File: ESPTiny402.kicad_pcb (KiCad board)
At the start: 2 copper layers, 26.4 x 23.9 mm, 20 parts, among them J1 Conn_01x10_Male, J2 Conn_01x10_Male, J3 Conn_01x04_Male, U1 ESP-01v090, U2 ATtiny402-SS, U3 MCP1700

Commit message: Minor layout changes
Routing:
- net GND: track 125.0 -> 119.9 mm

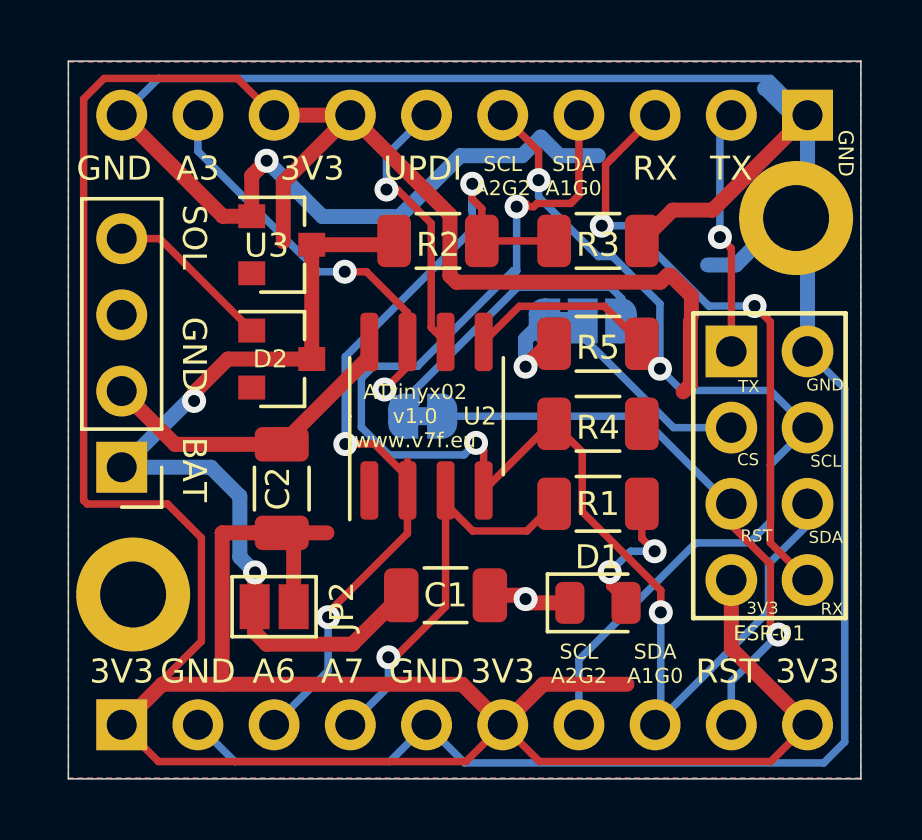
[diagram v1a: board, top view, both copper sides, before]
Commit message: Led to 1206 size
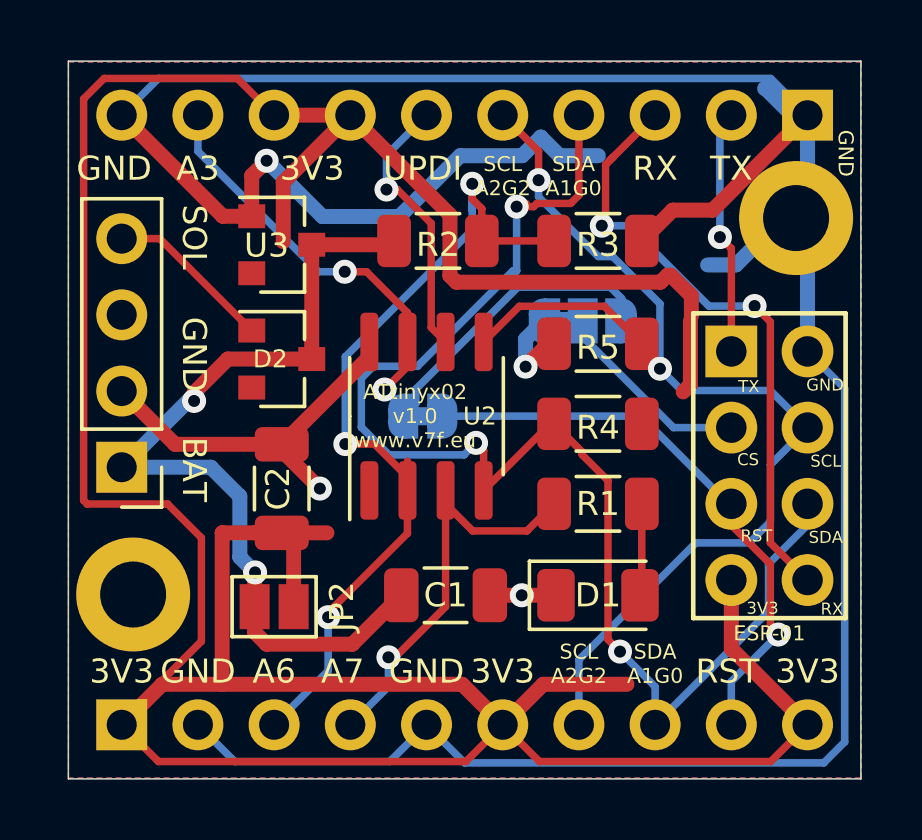
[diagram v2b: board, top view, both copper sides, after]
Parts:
- D1: footprint LED_SMD:LED_0805_2012Metric -> LED_SMD:LED_1206_3216Metric
- moved D1 0.25 mm to (63.4, 58.2)
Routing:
- net Net-(D1-Pad2): track 4.79 -> 3.07 mm, vias 2 -> 0
- net GND: track 119.9 -> 121.3 mm, vias 2 -> 3

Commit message: Minor routing updates
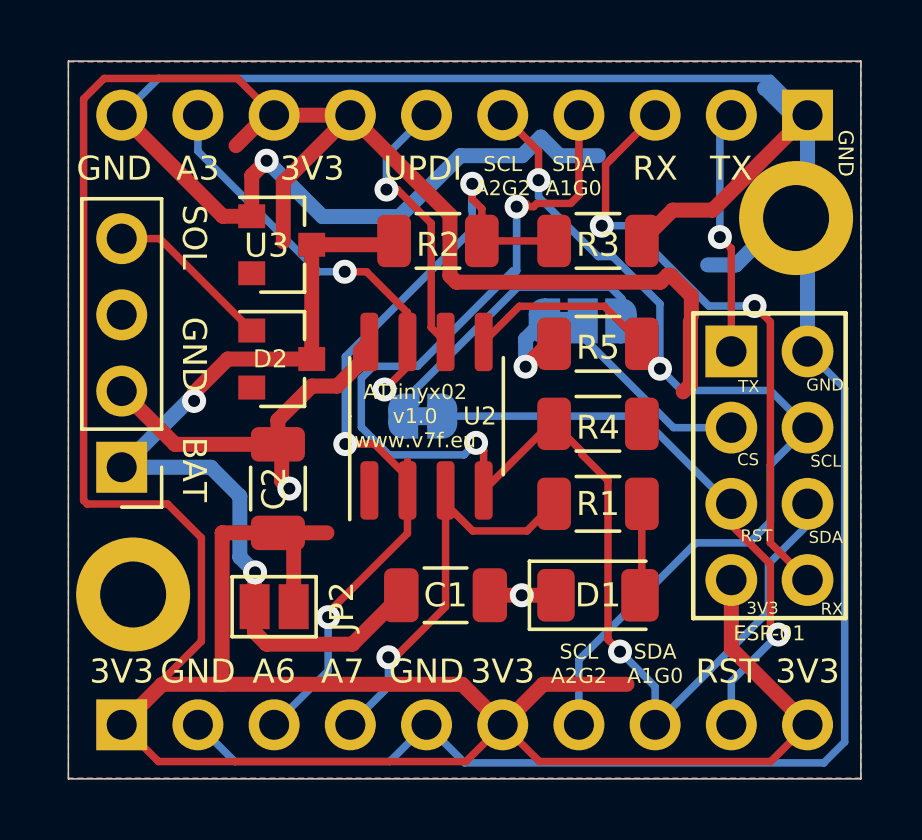
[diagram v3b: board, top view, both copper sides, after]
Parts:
- moved C2 0.13 mm to (52.7, 54.6)
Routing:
- net +3V3: track 123.0 -> 124.7 mm
- net GND: track 121.3 -> 122.1 mm
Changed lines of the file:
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@@
     (thickness 1.6)
     (drawings 55)
-    (tracks 271)
+    (tracks 279)
     (zones 0)
     (modules 20)
@@
   )
   (module Capacitor_SMD:C_1206_3216Metric (layer F.Cu)
-    (at 52.832 54.61 90)
+    (at 52.705 54.61 90)
     (descr "Capacitor SMD 1206 (3216 Metric), square (rectangular) end terminal, IPC_7351 nominal, (Body size source: IPC-SM-782 page 76, https://www.pcb-3d.com/wordpress/wp-content/uploads/ipc-sm-782a_amendment_1_and_2.pdf), generated with kicad-footprint-generator")
     (tags capacitor)
@@
   (segment (start 47.498 51.3588) (end 49.2742 53.135) (width 0.5) (layer F.Cu) (net 1) (status 10))
   (segment (start 55.753 50.214) (end 55.753 49.722) (width 0.5) (layer F.Cu) (net 1) (status 30))
-  (segment (start 52.832 53.135) (end 55.753 50.214) (width 0.5) (layer F.Cu) (net 1) (status 30))
   (segment (start 50.866 45.532) (end 51.832 45.532) (width 0.5) (layer F.Cu) (net 1) (status 20))
   (segment (start 47.498 42.164) (end 50.866 45.532) (width 0.5) (layer F.Cu) (net 1) (status 10))
@@
   (segment (start 59.768 58.166) (end 60.833 58.166) (width 0.5) (layer F.Cu) (net 1))
   (segment (start 60.833 58.166) (end 61.973 58.166) (width 0.5) (layer F.Cu) (net 1))
-  (via (at 54.102 54.61) (size 0.8) (drill 0.4) (layers F.Cu B.Cu) (net 1))
-  (segment (start 52.832 53.34) (end 54.102 54.61) (width 0.5) (layer F.Cu) (net 1))
+  (via (at 53.086 54.61) (size 0.8) (drill 0.4) (layers F.Cu B.Cu) (net 1))
   (segment (start 52.832 53.135) (end 52.832 53.34) (width 0.5) (layer F.Cu) (net 1))
+  (segment (start 52.832 54.356) (end 53.086 54.61) (width 0.5) (layer F.Cu) (net 1))
+  (segment (start 52.832 53.135) (end 52.832 54.356) (width 0.5) (layer F.Cu) (net 1))
+  (segment (start 55.453 50.421002) (end 54.682001 51.192001) (width 0.5) (layer F.Cu) (net 1))
+  (segment (start 55.453 50.022) (end 55.453 50.421002) (width 0.5) (layer F.Cu) (net 1))
+  (segment (start 55.753 49.722) (end 55.453 50.022) (width 0.5) (layer F.Cu) (net 1))
+  (segment (start 54.682001 51.192001) (end 53.836999 51.192001) (width 0.5) (layer F.Cu) (net 1))
+  (segment (start 52.705 52.324) (end 52.705 53.135) (width 0.5) (layer F.Cu) (net 1))
+  (segment (start 53.836999 51.192001) (end 52.705 52.324) (width 0.5) (layer F.Cu) (net 1))
   (segment (start 61.9105 49.784) (end 62.1685 49.784) (width 0.5) (layer F.Cu) (net 2) (status 30))
   (segment (start 52.832 56.085) (end 54.34 56.085) (width 0.5) (layer F.Cu) (net 2) (status 10))
@@
   (segment (start 47.498 62.357) (end 50.154001 59.700999) (width 0.25) (layer F.Cu) (net 2) (status 10))
   (segment (start 47.498 62.484) (end 47.498 62.357) (width 0.25) (layer F.Cu) (net 2) (status 30))
+  (segment (start 52.578 42.164) (end 52.324 42.164) (width 0.5) (layer F.Cu) (net 2))
+  (segment (start 52.324 42.164) (end 51.308 43.18) (width 0.5) (layer F.Cu) (net 2))
   (segment (start 64.8355 58.1035) (end 64.773 58.166) (width 0.25) (layer F.Cu) (net 4) (status 30))
   (segment (start 64.8355 55.118) (end 64.8355 58.1035) (width 0.25) (layer F.Cu) (net 4) (status 30))

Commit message: Minor routing updates
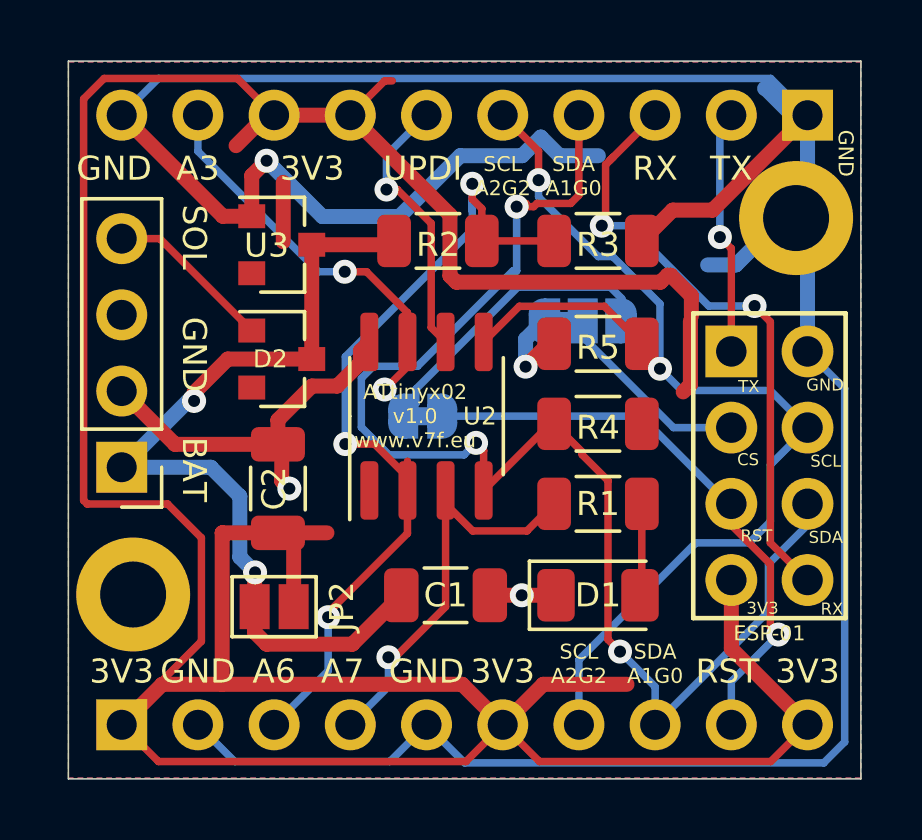
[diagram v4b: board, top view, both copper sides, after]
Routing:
- net +3V3: track 124.7 -> 123.4 mm
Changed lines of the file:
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@@
     (thickness 1.6)
     (drawings 55)
-    (tracks 279)
+    (tracks 280)
     (zones 0)
     (modules 20)
@@
   )
   (layers
-    (0 F.Cu signal)
+    (0 F.Cu signal hide)
     (31 B.Cu signal)
     (32 B.Adhes user)
@@
   (segment (start 64.8355 46.355) (end 65.862501 45.327999) (width 0.5) (layer F.Cu) (net 1) (status 10))
   (via (at 60.833 58.166) (size 0.8) (drill 0.4) (layers F.Cu B.Cu) (net 1))
-  (segment (start 59.768 58.166) (end 60.833 58.166) (width 0.5) (layer F.Cu) (net 1))
-  (segment (start 60.833 58.166) (end 61.973 58.166) (width 0.5) (layer F.Cu) (net 1))
+  (segment (start 59.768 58.166) (end 60.833 58.166) (width 0.5) (layer F.Cu) (net 1) (status 10))
+  (segment (start 60.833 58.166) (end 61.973 58.166) (width 0.5) (layer F.Cu) (net 1) (status 20))
   (via (at 53.086 54.61) (size 0.8) (drill 0.4) (layers F.Cu B.Cu) (net 1))
-  (segment (start 52.832 53.135) (end 52.832 53.34) (width 0.5) (layer F.Cu) (net 1))
+  (segment (start 52.832 53.135) (end 52.832 53.34) (width 0.5) (layer F.Cu) (net 1) (status 30))
   (segment (start 52.832 54.356) (end 53.086 54.61) (width 0.5) (layer F.Cu) (net 1))
-  (segment (start 52.832 53.135) (end 52.832 54.356) (width 0.5) (layer F.Cu) (net 1))
-  (segment (start 55.453 50.421002) (end 54.682001 51.192001) (width 0.5) (layer F.Cu) (net 1))
-  (segment (start 55.453 50.022) (end 55.453 50.421002) (width 0.5) (layer F.Cu) (net 1))
-  (segment (start 55.753 49.722) (end 55.453 50.022) (width 0.5) (layer F.Cu) (net 1))
+  (segment (start 52.832 53.135) (end 52.832 54.356) (width 0.5) (layer F.Cu) (net 1) (status 10))
+  (segment (start 55.453 50.421002) (end 54.682001 51.192001) (width 0.5) (layer F.Cu) (net 1) (status 10))
+  (segment (start 55.453 50.022) (end 55.453 50.421002) (width 0.5) (layer F.Cu) (net 1) (status 30))
+  (segment (start 55.753 49.722) (end 55.453 50.022) (width 0.5) (layer F.Cu) (net 1) (status 30))
   (segment (start 54.682001 51.192001) (end 53.836999 51.192001) (width 0.5) (layer F.Cu) (net 1))
-  (segment (start 52.705 52.324) (end 52.705 53.135) (width 0.5) (layer F.Cu) (net 1))
+  (segment (start 52.705 52.324) (end 52.705 53.135) (width 0.5) (layer F.Cu) (net 1) (status 20))
   (segment (start 53.836999 51.192001) (end 52.705 52.324) (width 0.5) (layer F.Cu) (net 1))
   (segment (start 61.9105 49.784) (end 62.1685 49.784) (width 0.5) (layer F.Cu) (net 2) (status 30))
@@
   (segment (start 52.578 42.164) (end 55.118 42.164) (width 0.5) (layer F.Cu) (net 2) (status 30))
   (segment (start 52.881999 44.400001) (end 52.881999 46.382001) (width 0.5) (layer F.Cu) (net 2))
-  (segment (start 55.118 42.164) (end 52.881999 44.400001) (width 0.5) (layer F.Cu) (net 2) (status 10))
   (segment (start 66.454399 51.147601) (end 66.454399 49.022) (width 0.5) (layer F.Cu) (net 2))
   (segment (start 66.21351 51.38849) (end 66.454399 51.147601) (width 0.5) (layer F.Cu) (net 2))
@@
   (segment (start 47.498 62.357) (end 50.154001 59.700999) (width 0.25) (layer F.Cu) (net 2) (status 10))
   (segment (start 47.498 62.484) (end 47.498 62.357) (width 0.25) (layer F.Cu) (net 2) (status 30))
-  (segment (start 52.578 42.164) (end 52.324 42.164) (width 0.5) (layer F.Cu) (net 2))
-  (segment (start 52.324 42.164) (end 51.308 43.18) (width 0.5) (layer F.Cu) (net 2))
+  (segment (start 52.578 42.164) (end 52.324 42.164) (width 0.5) (layer F.Cu) (net 2) (status 30))
+  (segment (start 52.324 42.164) (end 51.308 43.18) (width 0.5) (layer F.Cu) (net 2) (status 10))
+  (segment (start 55.118 42.164) (end 56.261 41.021) (width 0.25) (layer F.Cu) (net 2) (status 10))
+  (segment (start 56.261 41.021) (end 56.515 41.021) (width 0.25) (layer F.Cu) (net 2))
   (segment (start 64.8355 58.1035) (end 64.773 58.166) (width 0.25) (layer F.Cu) (net 4) (status 30))
   (segment (start 64.8355 55.118) (end 64.8355 58.1035) (width 0.25) (layer F.Cu) (net 4) (status 30))
